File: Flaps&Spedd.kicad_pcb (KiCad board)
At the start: 2 copper layers, 46 x 46 mm, 21 parts, among them J1 CAN-In, J2 CAN-Out, U1 SN65HVD230

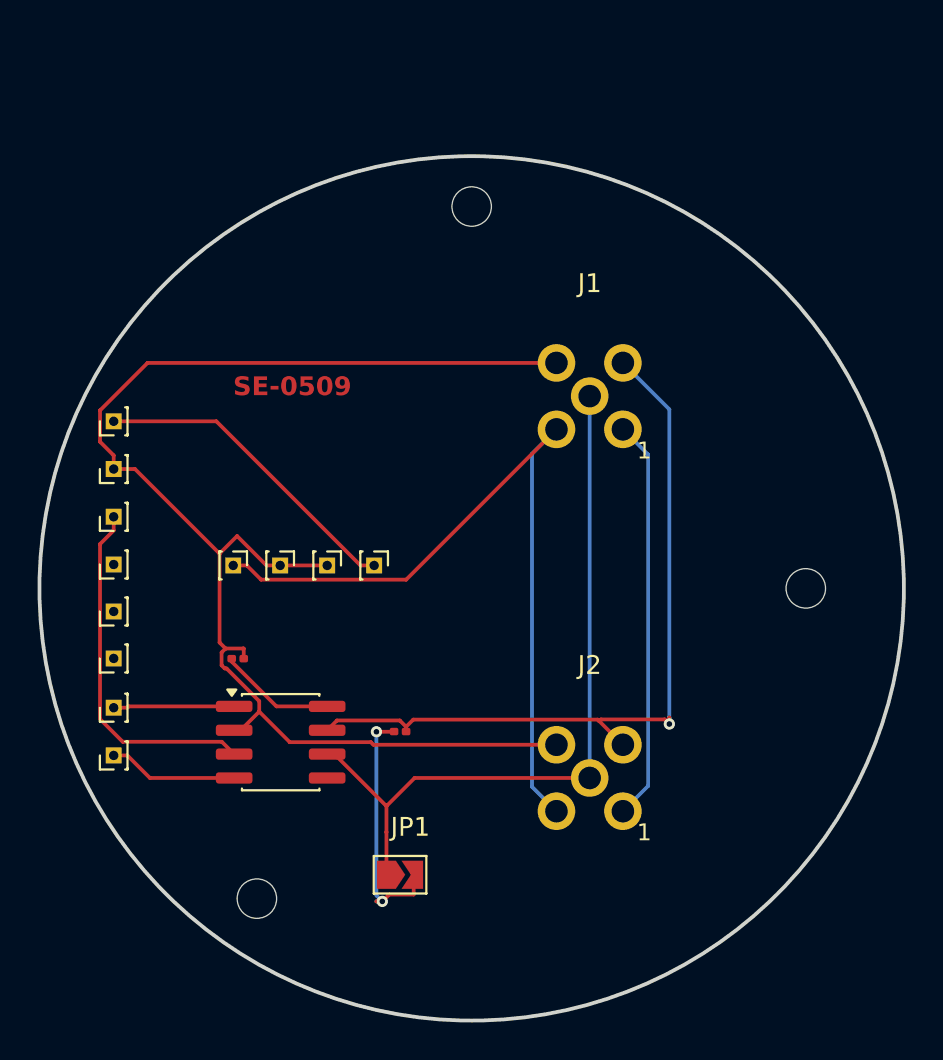
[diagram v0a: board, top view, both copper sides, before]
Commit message: Change to PinHeader_1x01_P1.27mm_Vertical, add C1.
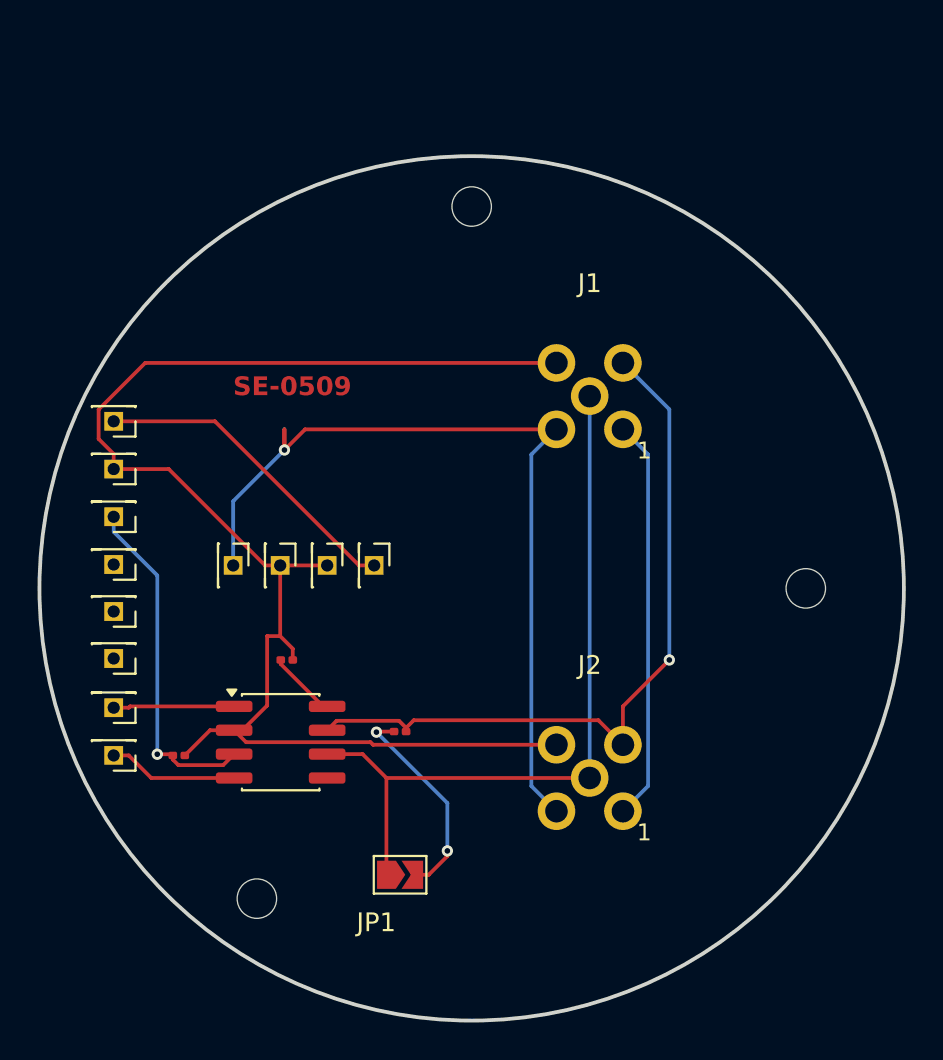
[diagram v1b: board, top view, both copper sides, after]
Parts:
- added C1: 100nF, Capacitor_SMD:C_0201_0603Metric, F.Cu at (60.6, 85.1)
- H1, H10, H11, H12, H13, H14, H2, H3, H4, H7, H8, H9: footprint Connector_PinHeader_1.00mm:PinHeader_1x01_P1.00mm_Vertical -> Connector_PinHeader_1.27mm:PinHeader_1x01_P1.27mm_Vertical
- moved R1 2.61 mm to (66.4, 80.0)
- turned H10 to 180 degrees
- turned H11 to 180 degrees
- turned H12 to 180 degrees
- turned H13 to 180 degrees
- turned H14 to 180 degrees
- turned H7 to 180 degrees
- turned H8 to 180 degrees
- turned H9 to 180 degrees
- renumbered REF** to MH1, REF** to MH2, REF** to MH3
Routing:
- net +12V: track 42.2 -> 48.0 mm, vias 0 -> 1
- net Net-(J1-Pin_4): track 42.6 -> 39.4 mm
- net Net-(JP1-B): track 14.2 -> 11.3 mm
- net GND: track 72.3 -> 75.0 mm
- net Net-(U1-Rs): track 6.23 -> 3.62 mm
- net +3V3: track 19.0 -> 18.3 mm, vias 0 -> 1

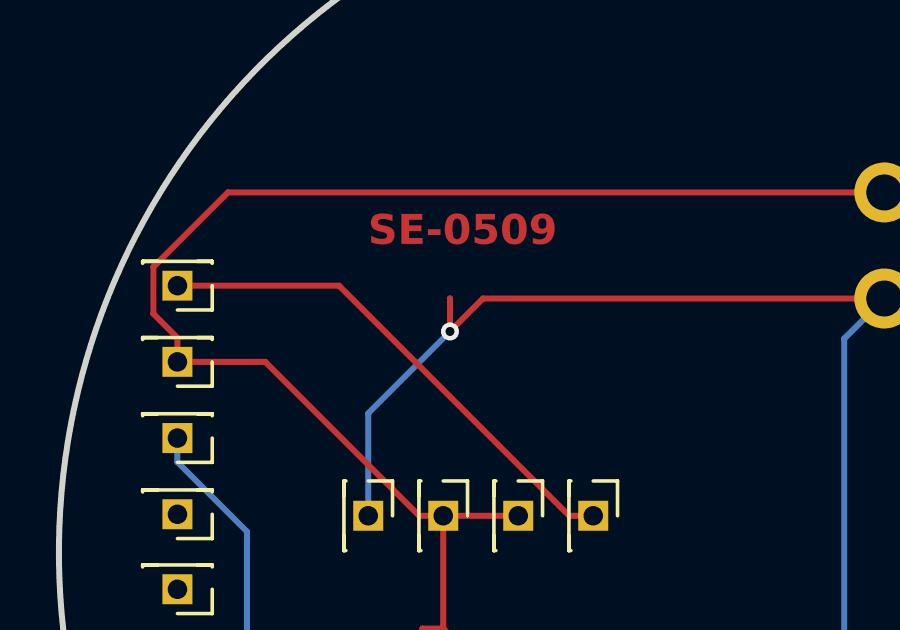
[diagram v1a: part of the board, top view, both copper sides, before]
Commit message: Wrong CAN connector placement, mirrored!
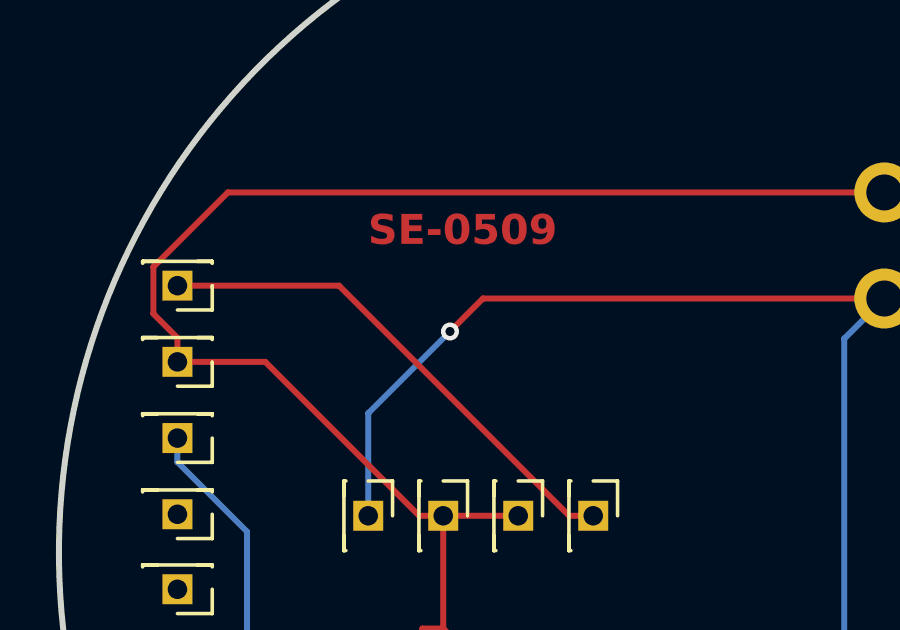
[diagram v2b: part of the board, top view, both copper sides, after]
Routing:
- net +12V: track 48.0 -> 43.6 mm
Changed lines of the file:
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@@
 		(sheetname "/")
 		(sheetfile "Flaps&Spedd.kicad_sch")
-		(attr through_hole exclude_from_bom)
+		(attr through_hole)
 		(fp_line
 			(start 1.16 0.81)
@@
 		(sheetname "/")
 		(sheetfile "Flaps&Spedd.kicad_sch")
-		(attr through_hole exclude_from_bom)
+		(attr through_hole)
 		(fp_line
 			(start 1.16 0.81)
@@
 		(sheetname "/")
 		(sheetfile "Flaps&Spedd.kicad_sch")
-		(attr through_hole exclude_from_bom)
+		(attr through_hole)
 		(fp_line
 			(start 1.16 0.81)
@@
 		(sheetname "/")
 		(sheetfile "Flaps&Spedd.kicad_sch")
-		(attr through_hole exclude_from_bom)
+		(attr through_hole)
 		(fp_line
 			(start 1.16 0.81)
@@
 		(sheetname "/")
 		(sheetfile "Flaps&Spedd.kicad_sch")
-		(attr through_hole exclude_from_bom)
+		(attr through_hole)
 		(fp_line
 			(start -1.16 0.81)
@@
 		(sheetname "/")
 		(sheetfile "Flaps&Spedd.kicad_sch")
-		(attr through_hole exclude_from_bom)
+		(attr through_hole)
 		(fp_line
 			(start -1.16 0.81)
@@
 		(sheetname "/")
 		(sheetfile "Flaps&Spedd.kicad_sch")
-		(attr through_hole)
+		(attr through_hole exclude_from_bom)
 		(fp_circle
 			(center 0 0)
@@
 		(sheetname "/")
 		(sheetfile "Flaps&Spedd.kicad_sch")
-		(attr through_hole exclude_from_bom)
+		(attr through_hole)
 		(fp_line
 			(start 1.16 0.81)
@@
 		(sheetname "/")
 		(sheetfile "Flaps&Spedd.kicad_sch")
-		(attr through_hole exclude_from_bom)
+		(attr through_hole)
 		(fp_line
 			(start 1.16 0.81)
@@
 		(sheetname "/")
 		(sheetfile "Flaps&Spedd.kicad_sch")
-		(attr through_hole)
+		(attr through_hole exclude_from_bom)
 		(fp_circle
 			(center 0 0)
@@
 		(sheetname "/")
 		(sheetfile "Flaps&Spedd.kicad_sch")
-		(attr through_hole exclude_from_bom)
+		(attr through_hole)
 		(fp_line
 			(start 1.16 0.81)
@@
 		(sheetname "/")
 		(sheetfile "Flaps&Spedd.kicad_sch")
-		(attr through_hole exclude_from_bom)
+		(attr through_hole)
 		(fp_line
 			(start -1.16 0.81)
@@
 		(sheetname "/")
 		(sheetfile "Flaps&Spedd.kicad_sch")
-		(attr through_hole exclude_from_bom)
+		(attr through_hole)
 		(fp_line
 			(start -1.16 0.81)
@@
 		(sheetname "/")
 		(sheetfile "Flaps&Spedd.kicad_sch")
-		(attr through_hole exclude_from_bom)
+		(attr through_hole)
 		(fp_line
 			(start 1.16 0.81)
@@
 	)
 	(segment
-		(start 66.2354 68.8371)
-		(end 66.2354 67.7378)
-		(width 0.2)
-		(layer "F.Cu")
-		(net 13)
-	)
-	(segment
 		(start 80.7122 67.7378)
 		(end 67.3347 67.7378)
@@
 	)
 	(segment
-		(start 66.2354 67.7378)
-		(end 66.2354 68.8371)
-		(width 0.2)
-		(layer "F.Cu")
-		(net 13)
-	)
-	(segment
 		(start 67.3347 67.7378)
 		(end 66.2354 68.8371)
@@
 		(net 13)
 	)
-	(segment
-		(start 66.2354 68.8371)
-		(end 66.2354 67.7378)
-		(width 0.2)
-		(layer "B.Cu")
-		(net 13)
-	)
-	(segment
-		(start 66.2354 67.7378)
-		(end 66.2354 68.8371)
-		(width 0.2)
-		(layer "B.Cu")
-		(net 13)
-	)

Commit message: Add comment.
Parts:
- J1: value CAN-In -> CAN-M
- J2: value CAN-Out -> CAN-F; moved to B.Cu
- turned J2 to 180 degrees
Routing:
- net Net-(JP1-B): track 11.3 -> 17.8 mm, vias 2 -> 0
- net Net-(J1-Pin_1): track 21.4 -> 27.5 mm
- net GND: track 75.0 -> 81.0 mm
- net +3V3: track 18.3 -> 22.1 mm
- net +12V: track 43.6 -> 45.9 mm, vias 1 -> 2
- net Net-(U1-Rs): track 3.62 -> 4.91 mm
- net Net-(J1-Pin_4): track 39.4 -> 40.1 mm, vias 1 -> 0
